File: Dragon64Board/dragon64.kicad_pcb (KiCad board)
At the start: 2 copper layers, 333.2 x 205.9 mm, 231 parts, among them IC1 74LS244, IC10 6847, IC11 6551, IC15 4164, IC16 4164, IC2 LM393, IC20 74LS273, IC21 4164, IC22 4164, IC25 74LS244, IC26 4164, IC27 4164, IC32 4164, IC33 4164, IC34 27C128, IC35 74LS00, IC36 74LS02, IC37 27C128, IC38 MC6809E, IC39 6883, IC4 4050, IC40 74LS138, IC5 6821, IC6 4529, IC7 4069, IC8 6821, J1 ATX, J2 TTL Serial Connector, J3 composite on luma, J4 DB9_Male, J5 DISK ROM ENABLE, J6 Floppy Interface, Q1 BC557, Q2 2N2222, Q3 2N2222, U1 MAX232, U10 WD2797, U2 MC1372, U3 74LS00, U4 74LS07, U5 27C64, U6 74LS04, U7 74LS139, U8 74LS06N, U9 74LS174, X1 14.31818Mhz, X3 4Mhz, Y2 1.8432Mhz

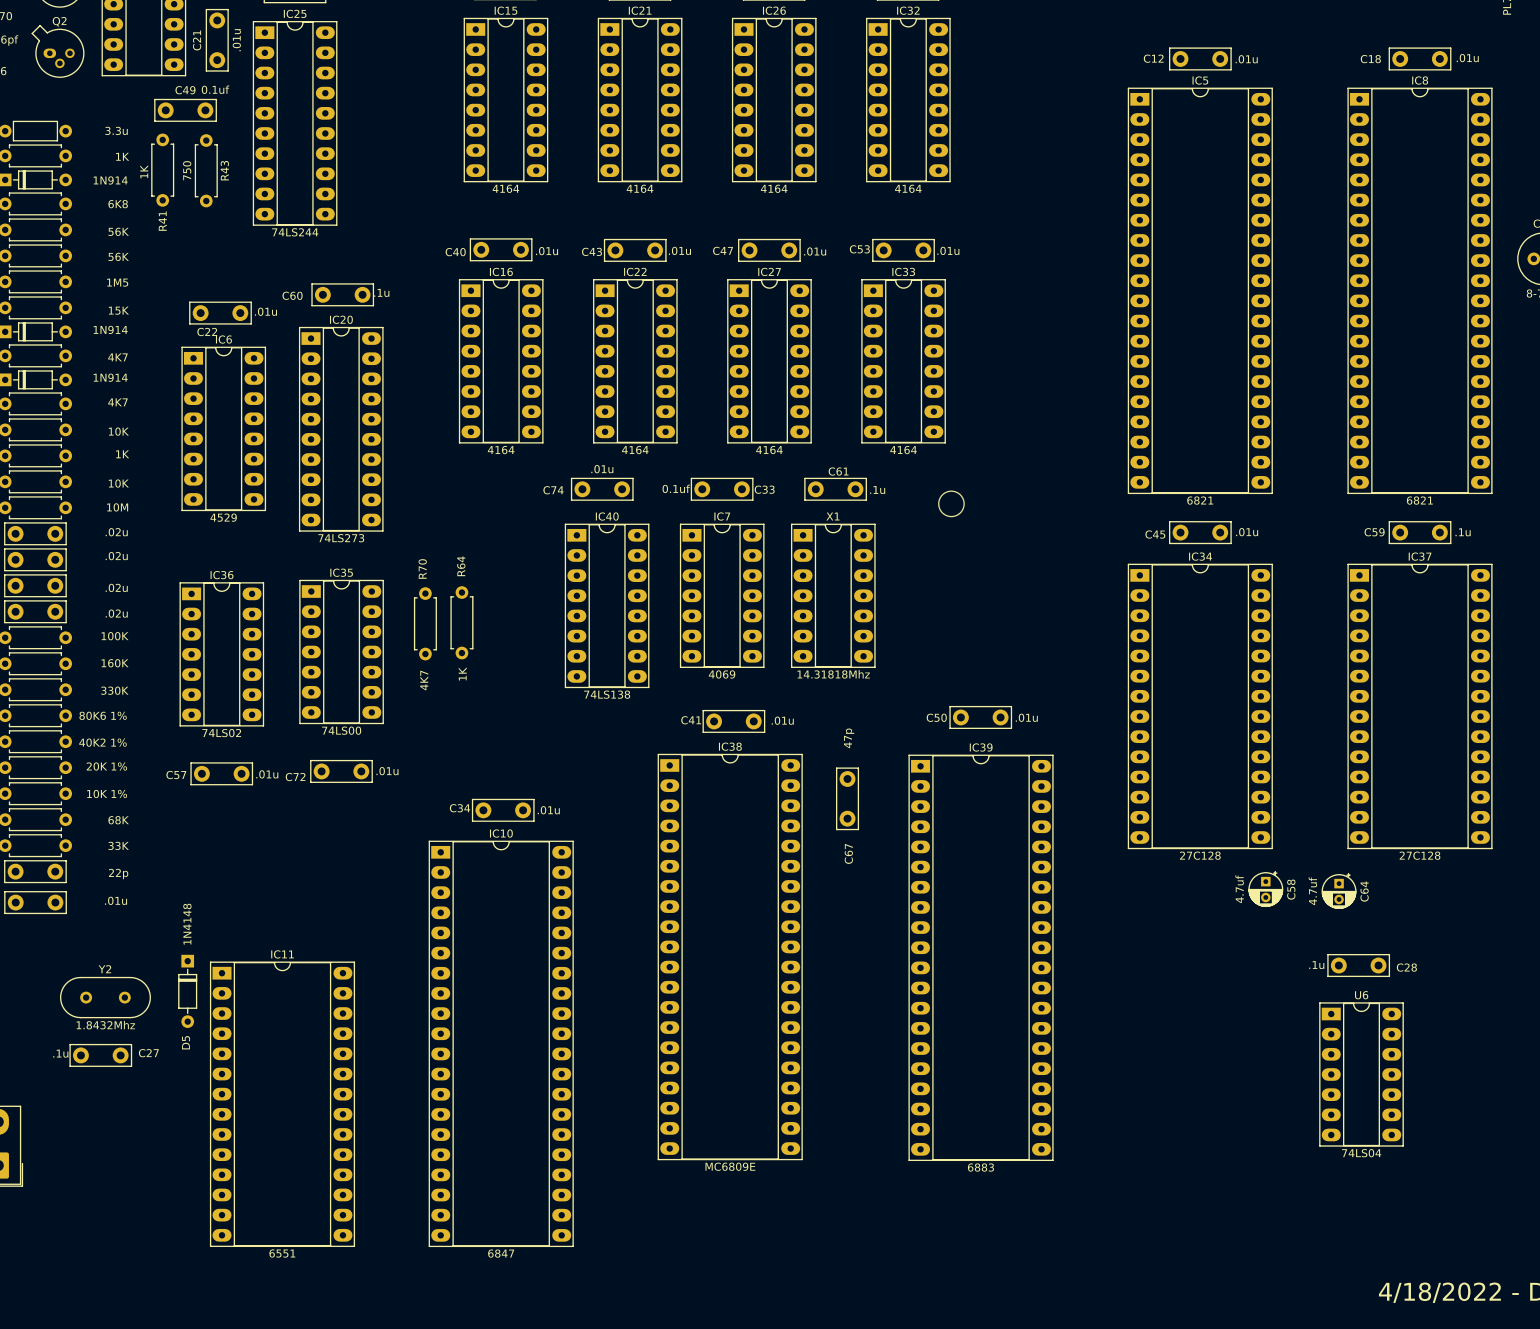
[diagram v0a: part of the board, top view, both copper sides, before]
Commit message: enclosure changes
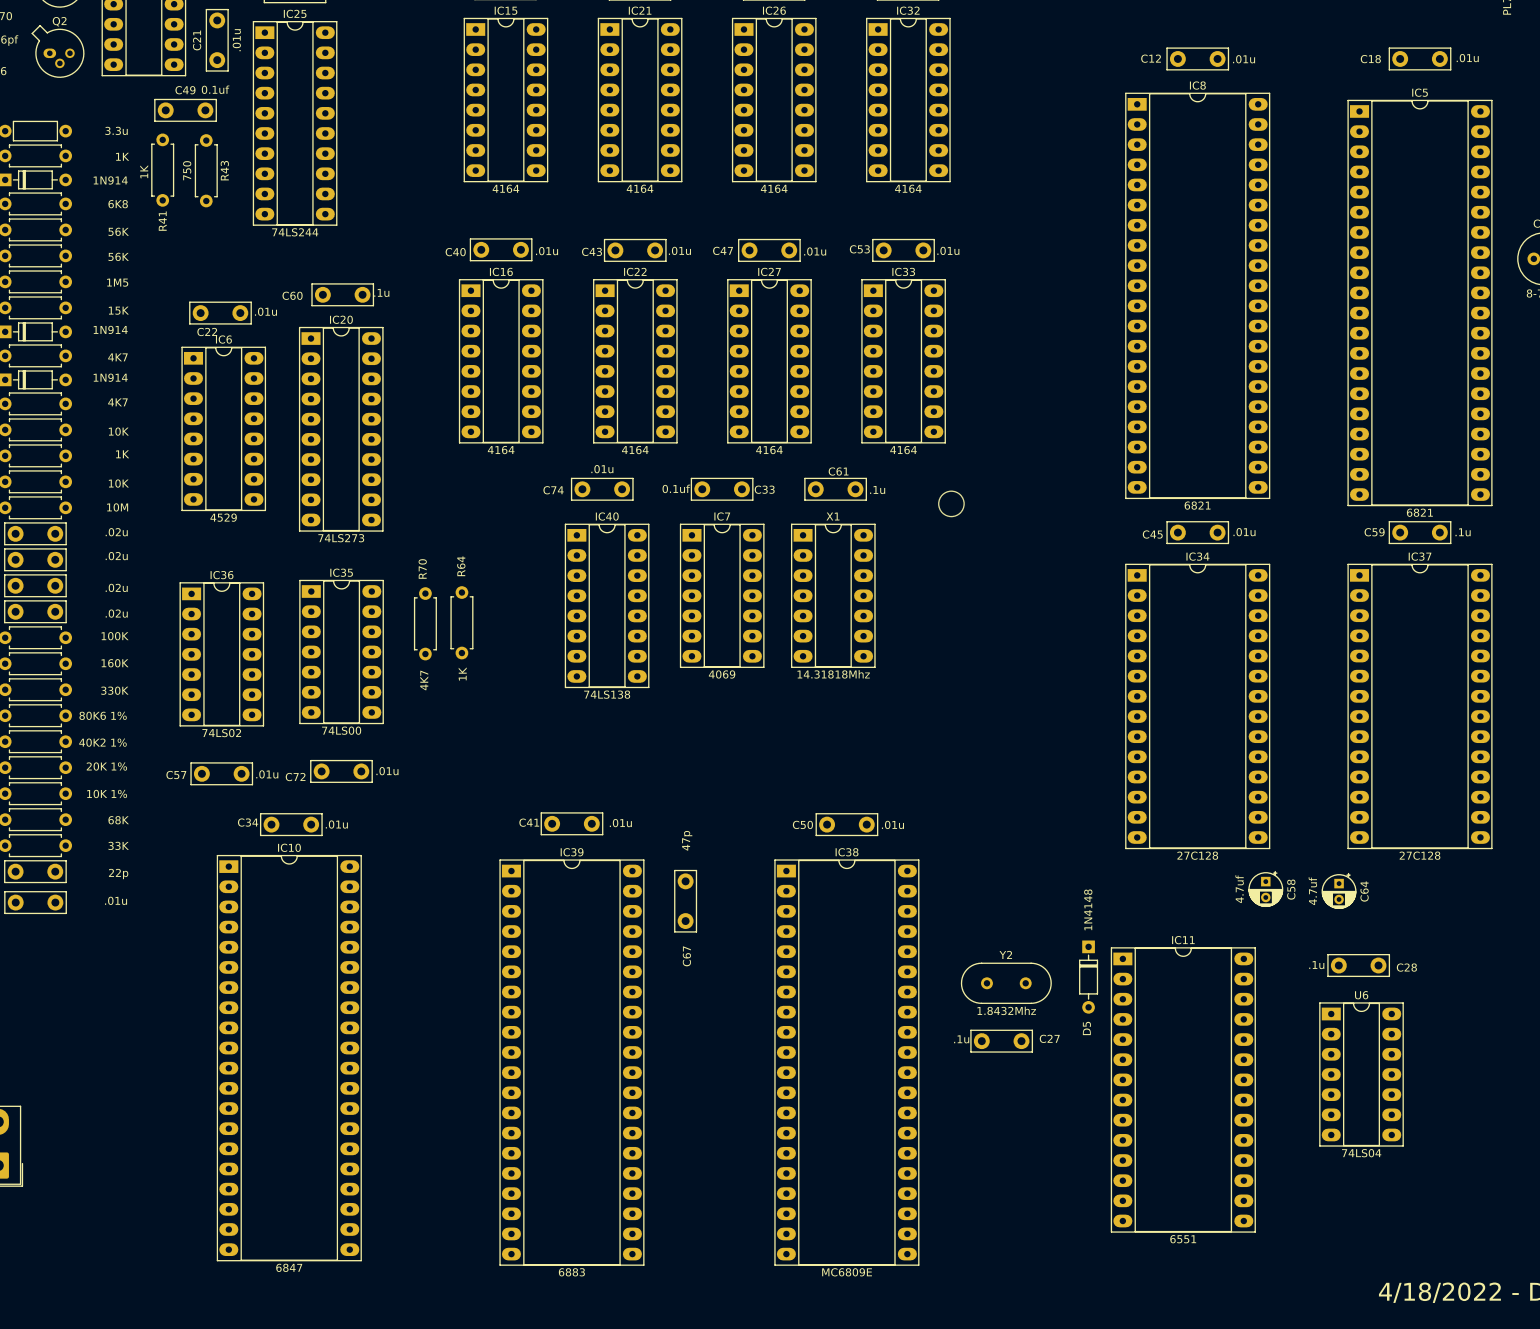
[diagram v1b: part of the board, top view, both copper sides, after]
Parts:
- moved IC11 113.5 mm to (199.5, 126.7)
- moved C27 113.5 mm to (181.7, 137.0)
- moved Y2 113.5 mm to (182.4, 129.7)
- moved D5 113.5 mm to (195.2, 125.2)
- moved IC39 53.2 mm to (122.5, 115.6)
- moved IC8 28.0 mm to (201.3, 19.0)
- moved IC5 27.7 mm to (229.3, 19.9)
- moved C34 26.8 mm to (92.2, 109.7)
- moved IC10 26.8 mm to (86.8, 115.0)
- moved C41 24.1 mm to (127.6, 109.6)
- moved C67 24.1 mm to (144.4, 121.9)
- moved C50 21.6 mm to (162.2, 109.7)
- moved IC38 19.8 mm to (157.1, 115.6)
- moved C12 0.33 mm to (206.4, 13.3)
- moved C45 0.33 mm to (206.4, 73.0)
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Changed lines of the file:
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@@
     (pad_to_mask_clearance 0)
     (aux_axis_origin 0 0)
-    (visible_elements 7EFFAEFF)
+    (visible_elements 7EFFA6FF)
     (pcbplotparams
       (layerselection 0x010fc_ffffffff)
@@
   )
   (module Diode_THT:D_DO-35_SOD27_P7.62mm_Horizontal (layer F.Cu)
-    (at 81.67 126.95 270)
+    (at 195.17 125.15 270)
     (descr "Diode, DO-35_SOD27 series, Axial, Horizontal, pin pitch=7.62mm, , length*diameter=4*2mm^2, , http://www.diodes.com/_files/packages/DO-35.pdf")
     (tags "Diode DO-35_SOD27 series Axial Horizontal pin pitch 7.62mm  length 4mm diameter 2mm")
@@
   )
   (module Crystal:Crystal_HC49-U_Vertical (layer F.Cu)
-    (at 68.87 131.54)
+    (at 182.37 129.74)
     (descr "Crystal THT HC-49/U http://5hertz.com/pdfs/04404_D.pdf")
     (tags "THT crystalHC-49/U")
@@
   )
   (module Package_DIP:DIP-40_W15.24mm_Socket_LongPads (layer F.Cu)
-    (at 174 102.4)
+    (at 122.46025 115.6)
     (descr "40-lead though-hole mounted DIP package, row spacing 15.24 mm (600 mils), Socket, LongPads")
     (tags "THT DIP DIL PDIP 2.54mm 15.24mm 600mil Socket LongPads")
@@
   )
   (module Package_DIP:DIP-40_W15.24mm_Socket_LongPads (layer F.Cu)
-    (at 142.4 102.3)
+    (at 157.1 115.6)
     (descr "40-lead though-hole mounted DIP package, row spacing 15.24 mm (600 mils), Socket, LongPads")
     (tags "THT DIP DIL PDIP 2.54mm 15.24mm 600mil Socket LongPads")
@@
   )
   (module Package_DIP:DIP-28_W15.24mm_Socket_LongPads (layer F.Cu)
-    (at 201.63 78.35)
+    (at 201.3 78.35)
     (descr "28-lead though-hole mounted DIP package, row spacing 15.24 mm (600 mils), Socket, LongPads")
     (tags "THT DIP DIL PDIP 2.54mm 15.24mm 600mil Socket LongPads")
@@
   )
   (module Package_DIP:DIP-28_W15.24mm_Socket_LongPads (layer F.Cu)
-    (at 85.99 128.47)
+    (at 199.49 126.67)
     (descr "28-lead though-hole mounted DIP package, row spacing 15.24 mm (600 mils), Socket, LongPads")
     (tags "THT DIP DIL PDIP 2.54mm 15.24mm 600mil Socket LongPads")
@@
   )
   (module Package_DIP:DIP-40_W15.24mm_Socket_LongPads (layer F.Cu)
-    (at 113.55 113.24)
+    (at 86.85 115.04)
     (descr "40-lead though-hole mounted DIP package, row spacing 15.24 mm (600 mils), Socket, LongPads")
     (tags "THT DIP DIL PDIP 2.54mm 15.24mm 600mil Socket LongPads")
@@
   )
   (module Package_DIP:DIP-40_W15.24mm_Socket_LongPads (layer F.Cu)
-    (at 229.305 18.368)
+    (at 201.3 19)
     (descr "40-lead though-hole mounted DIP package, row spacing 15.24 mm (600 mils), Socket, LongPads")
     (tags "THT DIP DIL PDIP 2.54mm 15.24mm 600mil Socket LongPads")
@@
   )
   (module Package_DIP:DIP-40_W15.24mm_Socket_LongPads (layer F.Cu)
-    (at 201.63 18.368)
+    (at 229.305 19.9)
     (descr "40-lead though-hole mounted DIP package, row spacing 15.24 mm (600 mils), Socket, LongPads")
     (tags "THT DIP DIL PDIP 2.54mm 15.24mm 600mil Socket LongPads")
@@
   )
   (module Capacitor_THT:C_Disc_D7.5mm_W2.5mm_P5.00mm (layer F.Cu)
-    (at 164.8 109 90)
+    (at 144.4 121.9 90)
     (descr "C, Disc series, Radial, pin pitch=5.00mm, , diameter*width=7.5*2.5mm^2, Capacitor, http://www.vishay.com/docs/28535/vy2series.pdf")
     (tags "C Disc series Radial pin pitch 5.00mm  diameter 7.5mm width 2.5mm Capacitor")
@@
   )
   (module Capacitor_THT:C_Disc_D7.5mm_W2.5mm_P5.00mm (layer F.Cu)
-    (at 179.0855 96.249)
+    (at 162.225 109.749)
     (descr "C, Disc series, Radial, pin pitch=5.00mm, , diameter*width=7.5*2.5mm^2, Capacitor, http://www.vishay.com/docs/28535/vy2series.pdf")
     (tags "C Disc series Radial pin pitch 5.00mm  diameter 7.5mm width 2.5mm Capacitor")
@@
   )
   (module Capacitor_THT:C_Disc_D7.5mm_W2.5mm_P5.00mm (layer F.Cu)
-    (at 206.755 72.959)
+    (at 206.425 72.959)
     (descr "C, Disc series, Radial, pin pitch=5.00mm, , diameter*width=7.5*2.5mm^2, Capacitor, http://www.vishay.com/docs/28535/vy2series.pdf")
     (tags "C Disc series Radial pin pitch 5.00mm  diameter 7.5mm width 2.5mm Capacitor")
@@
   )
   (module Capacitor_THT:C_Disc_D7.5mm_W2.5mm_P5.00mm (layer F.Cu)
-    (at 147.98525 96.749)
+    (at 127.58525 109.649)
     (descr "C, Disc series, Radial, pin pitch=5.00mm, , diameter*width=7.5*2.5mm^2, Capacitor, http://www.vishay.com/docs/28535/vy2series.pdf")
     (tags "C Disc series Radial pin pitch 5.00mm  diameter 7.5mm width 2.5mm Capacitor")
@@
   )
   (module Capacitor_THT:C_Disc_D7.5mm_W2.5mm_P5.00mm (layer F.Cu)
-    (at 118.925 107.949)
+    (at 92.225 109.749)
     (descr "C, Disc series, Radial, pin pitch=5.00mm, , diameter*width=7.5*2.5mm^2, Capacitor, http://www.vishay.com/docs/28535/vy2series.pdf")
     (tags "C Disc series Radial pin pitch 5.00mm  diameter 7.5mm width 2.5mm Capacitor")
@@
   )
   (module Capacitor_THT:C_Disc_D7.5mm_W2.5mm_P5.00mm (layer F.Cu)
-    (at 68.22 138.83)
+    (at 181.72 137.03)
     (descr "C, Disc series, Radial, pin pitch=5.00mm, , diameter*width=7.5*2.5mm^2, Capacitor, http://www.vishay.com/docs/28535/vy2series.pdf")
     (tags "C Disc series Radial pin pitch 5.00mm  diameter 7.5mm width 2.5mm Capacitor")
@@
   )
   (module Capacitor_THT:C_Disc_D7.5mm_W2.5mm_P5.00mm (layer F.Cu)
-    (at 206.755 13.285)
+    (at 206.425 13.285)
     (descr "C, Disc series, Radial, pin pitch=5.00mm, , diameter*width=7.5*2.5mm^2, Capacitor, http://www.vishay.com/docs/28535/vy2series.pdf")
     (tags "C Disc series Radial pin pitch 5.00mm  diameter 7.5mm width 2.5mm Capacitor")

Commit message: enclosure
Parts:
- removed PL7: Cartridge, dragon64:Edge_2x20_P2.54mm_Horizontal
- C2, C5, C68, C69: value .01u -> .1u
- moved R82 205.7 mm to (65.9, 135.7)
- moved R79 205.7 mm to (65.9, 126.7)
- moved R80 205.7 mm to (65.9, 129.7)
- moved R81 205.7 mm to (65.9, 132.7)
- moved R83 205.7 mm to (65.9, 138.6)
- moved R78 157.4 mm to (136.6, 148.2), turned to 0 degrees
- moved R77 156.8 mm to (136.6, 144.6), turned to 0 degrees
- moved R76 156.2 mm to (136.6, 141.0), turned to 0 degrees
- moved R75 155.6 mm to (136.6, 137.4), turned to 0 degrees
- moved C77 38.7 mm to (254.5, -0.10)
- moved R74 30.3 mm to (191.6, 20.2)
- moved R73 30.3 mm to (191.6, 17.2)
- moved U4 27.3 mm to (301.9, 104.3)
- moved U3 27.2 mm to (279.0, 88.4)
- moved R45 26.3 mm to (286.8, 148.1)
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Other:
- board text added: "4/30/2022 - Dan Werner Dragon/CoCo V0.5"
- board text removed: "4/18/2022 - Dan Werner Dragon/CoCo V0.5"

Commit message: enclosure
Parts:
- moved C74 194.0 mm to (324.5, 20.1)
- moved C33 183.0 mm to (318.7, -6.90)
- moved IC7 182.8 mm to (312.4, -0.50)
- moved IC15 137.6 mm to (157.7, 141.3)
- moved C39 137.6 mm to (159.0, 136.1)
- moved IC22 115.9 mm to (194.8, 141.3)
- moved C43 115.8 mm to (196.1, 136.1)
- moved C41 110.8 mm to (130.5, 0.35)
- moved C67 110.8 mm to (147.3, 12.6)
- moved IC39 110.8 mm to (125.4, 6.30)
- moved R75 110.8 mm to (148.5, 27.2)
- moved R76 110.8 mm to (148.5, 30.8)
- moved R77 110.8 mm to (148.5, 34.4)
- moved R78 110.8 mm to (148.5, 38.0)
- moved IC21 109.7 mm to (176.3, 111.2)
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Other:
- board text added: "5/4/2022 - Dan Werner Dragon/CoCo V0.5 May the 4th be with you. Always."
- board text removed: "4/30/2022 - Dan Werner Dragon/CoCo V0.5"

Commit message: enclosure
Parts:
- moved C46 191.0 mm to (82.2, 172.8)
- moved D5 168.0 mm to (78.1, 44.4)
- moved IC26 167.0 mm to (80.9, 149.7)
- moved C58 157.4 mm to (68.6, 167.9)
- moved C52 156.1 mm to (99.8, 172.9)
- moved R75 133.5 mm to (80.6, 142.2)
- moved IC10 132.5 mm to (170.8, 10.2)
- moved IC32 132.2 mm to (98.5, 149.7)
- moved R74 131.2 mm to (205.0, 142.2)
- moved R73 126.1 mm to (180.1, 142.2)
- moved R76 119.4 mm to (105.5, 142.2)
- moved C53 114.0 mm to (117.5, 172.7)
- moved X1 113.3 mm to (108.5, 11.3)
- moved C34 109.5 mm to (109.2, 6.10)
- moved R77 109.3 mm to (130.4, 142.2)
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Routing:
- net GND: track 0.00 -> 2421.4 mm
- net +5V: track 0.00 -> 2207.0 mm
- net ~RESET: track 0.00 -> 509.1 mm, vias 0 -> 4
- net E: track 0.00 -> 505.0 mm, vias 0 -> 5
- net /D4: track 0.00 -> 503.1 mm, vias 0 -> 3
- net /D5: track 0.00 -> 494.4 mm, vias 0 -> 1
- net R~W~: track 0.00 -> 471.5 mm, vias 0 -> 5
- net A1: track 0.00 -> 458.8 mm, vias 0 -> 2
- net /D7: track 0.00 -> 445.0 mm, vias 0 -> 1
- net /D6: track 0.00 -> 444.4 mm, vias 0 -> 2
- net +12V: track 0.00 -> 444.1 mm
- net /D0: track 0.00 -> 438.0 mm, vias 0 -> 4
- net /D3: track 0.00 -> 436.2 mm, vias 0 -> 3
- net A0: track 0.00 -> 435.0 mm, vias 0 -> 3
- net /PIAs/~ACK: track 0.00 -> 415.3 mm, vias 0 -> 2
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- added copper zone on B.Cu, net GND
- added copper zone on F.Cu, net GND
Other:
- net class V12 removed
- net class VCC: trace_width 1 -> 0.762

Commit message: add rom images
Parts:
- removed C2, C5, C68, C69: .1u, Capacitor_THT:C_Disc_D7.5mm_W2.5mm_P5.00mm
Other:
- board text added: "5/4/2022 - Dan Werner Dragon/CoCo V0.51 May the 4th be with you. Always."
- board text removed: "5/4/2022 - Dan Werner Dragon/CoCo V0.5 May the 4th be with you. Always."

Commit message: update schematic and enclosure
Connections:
- IC11 pad 18: /D0 -> D0
- IC11 pad 19: /D1 -> D1
- IC11 pad 20: /D2 -> D2
- IC11 pad 21: /D3 -> D3
- IC11 pad 22: /D4 -> D4
- IC11 pad 23: /D5 -> D5
- IC11 pad 24: /D6 -> D6
- IC11 pad 25: /D7 -> D7
- IC15 pad 2: /D7 -> D7
- IC16 pad 2: /D3 -> D3
- IC21 pad 2: /D6 -> D6
- IC22 pad 2: /D2 -> D2
- IC25 pad 12: /D6 -> D6
- IC25 pad 14: /D5 -> D5
- IC25 pad 16: /D2 -> D2
- IC25 pad 18: /D3 -> D3
- IC25 pad 3: /D4 -> D4
- IC25 pad 5: /D0 -> D0
- IC25 pad 7: /D1 -> D1
- IC25 pad 9: /D7 -> D7
- IC26 pad 2: /D5 -> D5
- IC27 pad 2: /D1 -> D1
- IC32 pad 2: /D4 -> D4
- IC33 pad 2: /D0 -> D0
- IC34 pad 11: /D0 -> D0
- IC34 pad 12: /D1 -> D1
- IC34 pad 13: /D2 -> D2
- IC34 pad 15: /D3 -> D3
- IC34 pad 16: /D4 -> D4
- IC34 pad 17: /D5 -> D5
- IC34 pad 18: /D6 -> D6
- IC34 pad 19: /D7 -> D7
- IC37 pad 11: /D0 -> D0
- IC37 pad 12: /D1 -> D1
- IC37 pad 13: /D2 -> D2
- IC37 pad 15: /D3 -> D3
- IC37 pad 16: /D4 -> D4
- IC37 pad 17: /D5 -> D5
- IC37 pad 18: /D6 -> D6
- IC37 pad 19: /D7 -> D7
- IC38 pad 24: /D7 -> D7
- IC38 pad 25: /D6 -> D6
- IC38 pad 26: /D5 -> D5
- IC38 pad 27: /D4 -> D4
- IC38 pad 28: /D3 -> D3
- IC38 pad 29: /D2 -> D2
- IC38 pad 30: /D1 -> D1
- IC38 pad 31: /D0 -> D0
- IC5 pad 26: /D7 -> D7
- IC5 pad 27: /D6 -> D6
- IC5 pad 28: /D5 -> D5
- IC5 pad 29: /D4 -> D4
- IC5 pad 30: /D3 -> D3
- IC5 pad 31: /D2 -> D2
- IC5 pad 32: /D1 -> D1
- IC5 pad 33: /D0 -> D0
- IC8 pad 26: /D7 -> D7
- IC8 pad 27: /D6 -> D6
- IC8 pad 28: /D5 -> D5
- IC8 pad 29: /D4 -> D4
- IC8 pad 30: /D3 -> D3
- IC8 pad 31: /D2 -> D2
- IC8 pad 32: /D1 -> D1
- IC8 pad 33: /D0 -> D0
- PL9 pad 10: /D0 -> D0
- PL9 pad 11: /D1 -> D1
- PL9 pad 12: /D2 -> D2
- PL9 pad 13: /D3 -> D3
- PL9 pad 14: /D4 -> D4
- PL9 pad 15: /D5 -> D5
- PL9 pad 16: /D6 -> D6
- PL9 pad 17: /D7 -> D7
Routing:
- net GND: track 2421.4 -> 0.00 mm
- net +5V: track 2207.0 -> 0.00 mm
- net ~RESET: track 509.1 -> 0.00 mm, vias 4 -> 0
- net E: track 505.0 -> 0.00 mm, vias 5 -> 0
- net /D4: track 503.1 -> 0.00 mm, vias 3 -> 0
- net /D5: track 494.4 -> 0.00 mm, vias 1 -> 0
- net R~W~: track 471.5 -> 0.00 mm, vias 5 -> 0
- net A1: track 458.8 -> 0.00 mm, vias 2 -> 0
- net /D7: track 445.0 -> 0.00 mm, vias 1 -> 0
- net /D6: track 444.4 -> 0.00 mm, vias 2 -> 0
- net +12V: track 444.1 -> 0.00 mm
- net /D0: track 438.0 -> 0.00 mm, vias 4 -> 0
- net /D3: track 436.2 -> 0.00 mm, vias 3 -> 0
- net A0: track 435.0 -> 0.00 mm, vias 3 -> 0
- net /PIAs/~ACK: track 415.3 -> 0.00 mm, vias 2 -> 0
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- removed copper zone on B.Cu, net GND
- removed copper zone on F.Cu, net GND
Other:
- board text added: "5/30/2022 - Dan Werner Dragon/CoCo V0.6"
- board text removed: "5/4/2022 - Dan Werner Dragon/CoCo V0.51 May the 4th be with you. Always."
